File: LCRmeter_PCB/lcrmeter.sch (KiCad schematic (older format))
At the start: 63 parts, among them J1 LCR_input, J2 LCR_input, J3 Prog_interface, J4 USB_B_Micro, J5 OSCILLOSCOPE, J6 misc, J7 misc, SW1 power, SW2 +, SW3 -, SW4 ok, SW5 back, U1 MCP47, U2 STM32F103C8Tx, U3 OLED, U4 74HC14, U5 MCP6001-OT, Y1 8Mhz

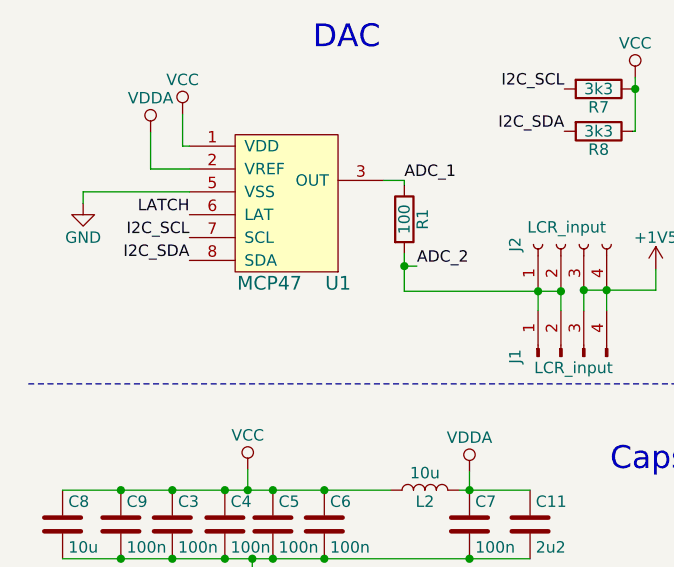
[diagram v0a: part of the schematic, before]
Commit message: SSD1306 final touches; MCP47 in 'safe' condition
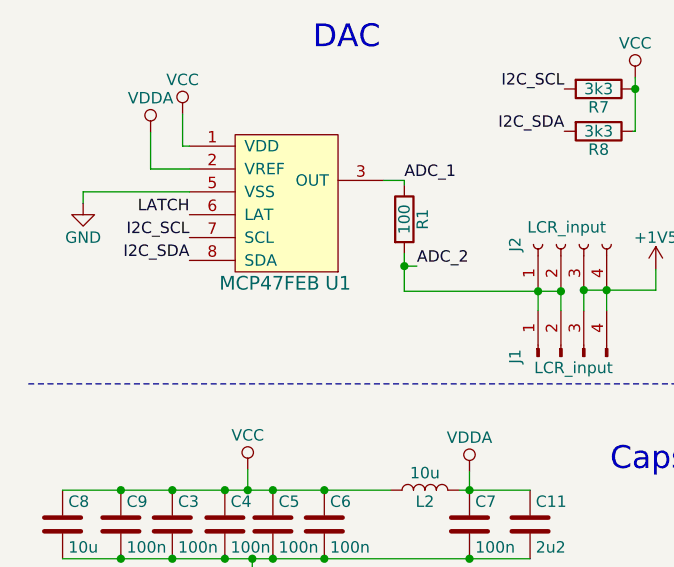
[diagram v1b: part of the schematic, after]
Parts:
- U1: value MCP47 -> MCP47FEB
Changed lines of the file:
@@
 P 1655 5930
 F 0 "U1" H 1855 5630 60  0000 C CNN
-F 1 "MCP47" H 1555 5630 60  0000 C CNN
+F 1 "MCP47FEB" H 1555 5630 60  0000 C CNN
 F 2 "Package_SO:TSSOP-8_4.4x3mm_P0.65mm" H 1955 5630 60  0001 C CNN
 F 3 "" H 1955 5630 60  0001 C CNN
